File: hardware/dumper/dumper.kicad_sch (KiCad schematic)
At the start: 17 parts, among them J1 /Reset, J10 arduino 10, J11 ss, J2 Clock In, J3 data, J4 clock, J5 2816 /WR disconnect, J6 arduino 13, J7 arduino 11, J8 arduino 5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

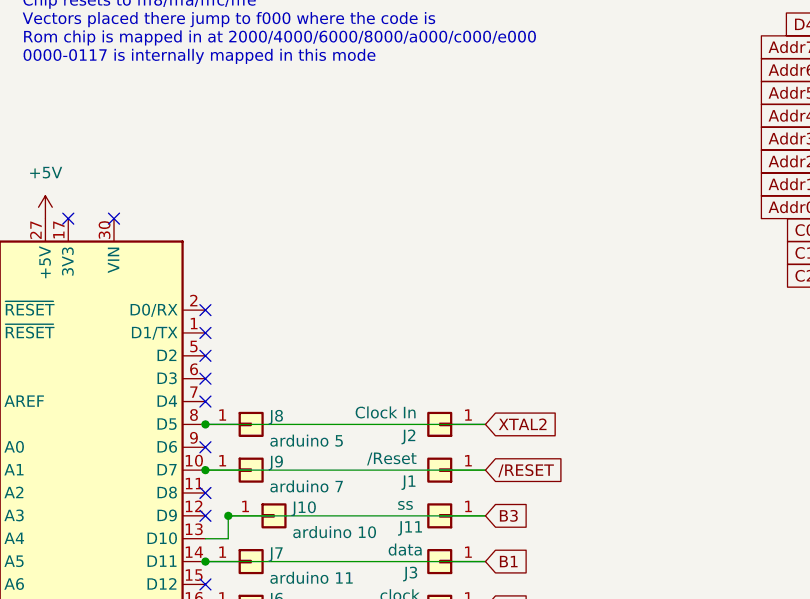
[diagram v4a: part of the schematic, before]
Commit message: added button and LED, still need software support though
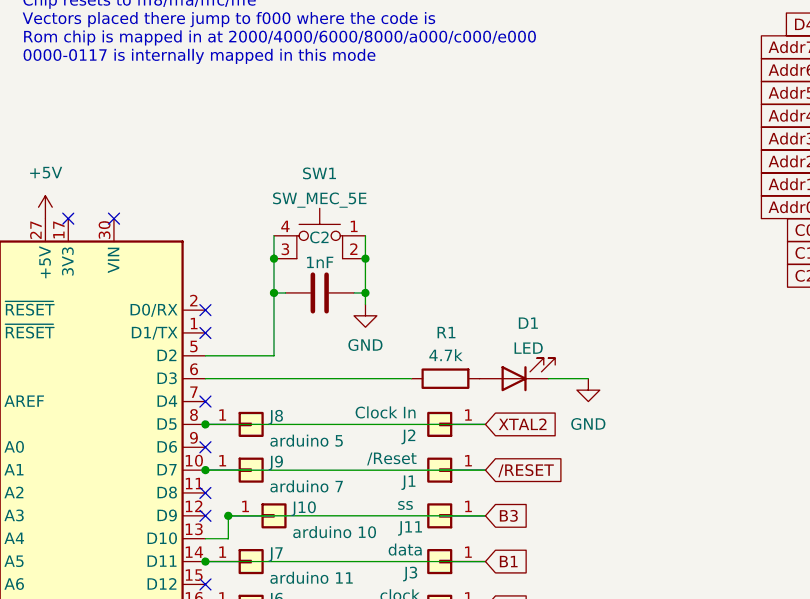
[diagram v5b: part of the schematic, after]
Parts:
- added C2: 1nF, Capacitor_THT:C_Axial_L3.8mm_D2.6mm_P7.50mm_Horizontal, symbol Device:C
- added D1: LED, LED_THT:LED_D5.0mm, symbol Device:LED
- added R1: 4.7k, Resistor_THT:R_Axial_DIN0207_L6.3mm_D2.5mm_P2.54mm_Vertical, symbol Device:R
- added SW1: SW_MEC_5E, Button_Switch_THT:SW_TH_Tactile_Omron_B3F-10xx, symbol Switch:SW_MEC_5E
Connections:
- net GND: now also C2.1, D1.1 (K), SW1.1, SW1.2
- net at A1.5 (D2): now also C2.2, SW1.3 (K), SW1.4 (A)
- net at A1.6 (D3): now also R1.1
- new net: D1.2 (A), R1.2
- no-connect marks 22 -> 20
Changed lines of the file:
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@@
   (junction (at 196.85 39.37) (diameter 0) (color 0 0 0 0)
   )
+  (junction (at 78.105 67.945) (diameter 0) (color 0 0 0 0)
+  )
   (junction (at 70.485 86.36) (diameter 0) (color 0 0 0 0)
   )
+  (junction (at 88.265 67.945) (diameter 0) (color 0 0 0 0)
+  )
   (junction (at 70.485 106.68) (diameter 0) (color 0 0 0 0)
   )
   (junction (at 70.485 91.44) (diameter 0) (color 0 0 0 0)
+  )
+  (junction (at 78.105 71.755) (diameter 0) (color 0 0 0 0)
+  )
+  (junction (at 88.265 71.755) (diameter 0) (color 0 0 0 0)
   )
   (junction (at 233.68 113.03) (diameter 0) (color 0 0 0 0)
@@
   (no_connect (at 70.485 93.98))
   (no_connect (at 70.485 96.52))
-  (no_connect (at 70.485 81.28))
-  (no_connect (at 70.485 78.74))
   (no_connect (at 70.485 83.82))
   (no_connect (at 60.325 63.5))
@@
     (stroke (width 0) (type default) (color 0 0 0 0))
   )
+  (wire (pts (xy 88.265 71.755) (xy 88.265 73.025))
+    (stroke (width 0) (type default) (color 0 0 0 0))
+  )
   (wire (pts (xy 70.485 106.68) (xy 101.6 106.68))
     (stroke (width 0) (type default) (color 0 0 0 0))
   )
+  (wire (pts (xy 88.265 65.405) (xy 88.265 67.945))
+    (stroke (width 0) (type default) (color 0 0 0 0))
+  )
+  (wire (pts (xy 78.105 71.755) (xy 78.105 67.945))
+    (stroke (width 0) (type default) (color 0 0 0 0))
+  )
   (wire (pts (xy 214.63 107.95) (xy 207.01 107.95))
     (stroke (width 0) (type default) (color 0 0 0 0))
@@
     (stroke (width 0) (type default) (color 0 0 0 0))
   )
+  (wire (pts (xy 78.105 78.74) (xy 70.485 78.74))
+    (stroke (width 0) (type default) (color 0 0 0 0))
+  )
   (wire (pts (xy 70.485 101.6) (xy 101.6 101.6))
     (stroke (width 0) (type default) (color 0 0 0 0))
@@
     (stroke (width 0) (type default) (color 0 0 0 0))
   )
+  (wire (pts (xy 78.105 65.405) (xy 78.105 67.945))
+    (stroke (width 0) (type default) (color 0 0 0 0))
+  )
   (wire (pts (xy 195.58 41.91) (xy 196.85 41.91))
     (stroke (width 0) (type default) (color 0 0 0 0))
   )
+  (wire (pts (xy 79.375 71.755) (xy 78.105 71.755))
+    (stroke (width 0) (type default) (color 0 0 0 0))
+  )
   (wire (pts (xy 139.7 36.195) (xy 139.7 39.37))
     (stroke (width 0) (type default) (color 0 0 0 0))
@@
   )
   (wire (pts (xy 55.245 121.285) (xy 55.245 114.3))
+    (stroke (width 0) (type default) (color 0 0 0 0))
+  )
+  (wire (pts (xy 88.265 71.755) (xy 86.995 71.755))
+    (stroke (width 0) (type default) (color 0 0 0 0))
+  )
+  (wire (pts (xy 93.345 81.28) (xy 70.485 81.28))
+    (stroke (width 0) (type default) (color 0 0 0 0))
+  )
+  (wire (pts (xy 113.03 81.28) (xy 108.585 81.28))
+    (stroke (width 0) (type default) (color 0 0 0 0))
+  )
+  (wire (pts (xy 88.265 67.945) (xy 88.265 71.755))
+    (stroke (width 0) (type default) (color 0 0 0 0))
+  )
+  (wire (pts (xy 78.105 71.755) (xy 78.105 78.74))
     (stroke (width 0) (type default) (color 0 0 0 0))
   )
@@
     (pin "2")
   )
+  (symbol (lib_id "Switch:SW_MEC_5E") (at 83.185 67.945 0) (mirror y) (unit 1)
+    (in_bom yes) (on_board yes) (fields_autoplaced)
+    (property "Reference" "SW1" (id 0) (at 83.185 58.5175 0))
+    (property "Value" "SW_MEC_5E" (id 1) (at 83.185 61.2926 0))
+    (property "Footprint" "Button_Switch_THT:SW_TH_Tactile_Omron_B3F-10xx" (id 2) (at 83.185 60.325 0)
+      (effects (font (size 1.27 1.27)) hide)
+    )
+    (property "Datasheet" "http://www.apem.com/int/index.php?controller=attachment&id_attachment=1371" (id 3) (at 83.185 60.325 0)
+      (effects (font (size 1.27 1.27)) hide)
+    )
+    (pin "1")
+    (pin "2")
+    (pin "3")
+    (pin "4")
+  )
   (symbol (lib_id "power:GND") (at 204.47 54.61 0) (unit 1)
     (in_bom yes) (on_board yes) (fields_autoplaced)
@@
     (pin "1")
   )
+  (symbol (lib_id "power:GND") (at 113.03 81.28 0) (unit 1)
+    (in_bom yes) (on_board yes) (fields_autoplaced)
+    (property "Reference" "#PWR0115" (id 0) (at 113.03 87.63 0)
+      (effects (font (size 1.27 1.27)) hide)
+    )
+    (property "Value" "GND" (id 1) (at 113.03 86.36 0))
+    (property "Footprint" "" (id 2) (at 113.03 81.28 0)
+      (effects (font (size 1.27 1.27)) hide)
+    )
+    (property "Datasheet" "" (id 3) (at 113.03 81.28 0)
+      (effects (font (size 1.27 1.27)) hide)
+    )
+    (pin "1")
+  )
   (symbol (lib_id "Connector_Generic:Conn_01x01") (at 75.565 106.68 0) (unit 1)
     (in_bom yes) (on_board yes) (fields_autoplaced)
@@
     )
     (pin "1")
+  )
+  (symbol (lib_id "Device:LED") (at 104.775 81.28 180) (unit 1)
+    (in_bom yes) (on_board yes) (fields_autoplaced)
+    (property "Reference" "D1" (id 0) (at 106.3625 75.1545 0))
+    (property "Value" "LED" (id 1) (at 106.3625 77.9296 0))
+    (property "Footprint" "LED_THT:LED_D5.0mm" (id 2) (at 104.775 81.28 0)
+      (effects (font (size 1.27 1.27)) hide)
+    )
+    (property "Datasheet" "~" (id 3) (at 104.775 81.28 0)
+      (effects (font (size 1.27 1.27)) hide)
+    )
+    (pin "1")
+    (pin "2")
   )
   (symbol (lib_id "power:+5V") (at 229.235 130.175 0) (unit 1)
@@
     )
     (pin "1")
+  )
+  (symbol (lib_id "Device:R") (at 97.155 81.28 90) (mirror x) (unit 1)
+    (in_bom yes) (on_board yes)
+    (property "Reference" "R1" (id 0) (at 98.425 76.2 90)
+      (effects (font (size 1.27 1.27)) (justify left))
+    )
+    (property "Value" "4.7k" (id 1) (at 99.06 78.74 90)
+      (effects (font (size 1.27 1.27)) (justify left))
+    )
+    (property "Footprint" "Resistor_THT:R_Axial_DIN0207_L6.3mm_D2.5mm_P2.54mm_Vertical" (id 2) (at 97.155 79.502 90)
+      (effects (font (size 1.27 1.27)) hide)
+    )
+    (property "Datasheet" "~" (id 3) (at 97.155 81.28 0)
+      (effects (font (size 1.27 1.27)) hide)
+    )
+    (pin "1")
+    (pin "2")
   )
   (symbol (lib_id "Connector_Generic:Conn_01x01") (at 96.52 101.6 180) (unit 1)
@@
     (pin "1")
   )
+  (symbol (lib_id "power:GND") (at 88.265 73.025 0) (mirror y) (unit 1)
+    (in_bom yes) (on_board yes) (fields_autoplaced)
+    (property "Reference" "#PWR0114" (id 0) (at 88.265 79.375 0)
+      (effects (font (size 1.27 1.27)) hide)
+    )
+    (property "Value" "GND" (id 1) (at 88.265 77.5875 0))
+    (property "Footprint" "" (id 2) (at 88.265 73.025 0)
+      (effects (font (size 1.27 1.27)) hide)
+    )
+    (property "Datasheet" "" (id 3) (at 88.265 73.025 0)
+      (effects (font (size 1.27 1.27)) hide)
+    )
+    (pin "1")
+  )
+  (symbol (lib_id "Device:C") (at 83.185 71.755 270) (mirror x) (unit 1)
+    (in_bom yes) (on_board yes) (fields_autoplaced)
+    (property "Reference" "C2" (id 0) (at 83.185 65.6295 90))
+    (property "Value" "1nF" (id 1) (at 83.185 68.4046 90))
+    (property "Footprint" "Capacitor_THT:C_Axial_L3.8mm_D2.6mm_P7.50mm_Horizontal" (id 2) (at 79.375 70.7898 0)
+      (effects (font (size 1.27 1.27)) hide)
+    )
+    (property "Datasheet" "~" (id 3) (at 83.185 71.755 0)
+      (effects (font (size 1.27 1.27)) hide)
+    )
+    (pin "1")
+    (pin "2")
+  )
   (symbol (lib_id "Connector_Generic:Conn_01x01") (at 96.52 106.68 180) (unit 1)
     (in_bom yes) (on_board yes)
@@
       (reference "#PWR0113") (unit 1) (value "+5V") (footprint "")
     )
+    (path "/caf3d6fa-4a2b-4403-b2a4-8ef75b254fa4"
+      (reference "#PWR0114") (unit 1) (value "GND") (footprint "")
+    )
+    (path "/1d761fca-95b7-43bf-972d-3e5ef51985f2"
+      (reference "#PWR0115") (unit 1) (value "GND") (footprint "")
+    )
     (path "/688ac639-00fc-4ac8-adf3-07f16d38668d"
       (reference "#PWR0116") (unit 1) (value "+5V") (footprint "")
@@
       (reference "C1") (unit 1) (value "0.1uF") (footprint "Capacitor_THT:C_Axial_L3.8mm_D2.6mm_P7.50mm_Horizontal")
     )
+    (path "/cbedcb1f-f6fd-4ef5-b1b7-a22936804498"
+      (reference "C2") (unit 1) (value "1nF") (footprint "Capacitor_THT:C_Axial_L3.8mm_D2.6mm_P7.50mm_Horizontal")
+    )
+    (path "/2fc6fbea-a5ac-44e1-ae14-5f7455ad4ad6"
+      (reference "D1") (unit 1) (value "LED") (footprint "LED_THT:LED_D5.0mm")
+    )
     (path "/8e871c2d-c01d-49fb-8a3b-6261894a19c0"
       (reference "J1") (unit 1) (value "/Reset") (footprint "Connector_PinHeader_2.54mm:PinHeader_1x01_P2.54mm_Vertical")
@@
       (reference "J11") (unit 1) (value "ss") (footprint "Connector_PinHeader_2.54mm:PinHeader_1x01_P2.54mm_Vertical")
     )
+    (path "/87fb4618-ffba-4098-894c-2a108e97e5a6"
+      (reference "R1") (unit 1) (value "4.7k") (footprint "Resistor_THT:R_Axial_DIN0207_L6.3mm_D2.5mm_P2.54mm_Vertical")
+    )
     (path "/010d4c25-3047-4e82-9722-4113a4b03be6"
       (reference "R2") (unit 1) (value "4.7k") (footprint "Resistor_THT:R_Axial_DIN0207_L6.3mm_D2.5mm_P2.54mm_Vertical")
     )
+    (path "/05b0e45b-bcdc-4c03-b4a1-c60becea55d5"
+      (reference "SW1") (unit 1) (value "SW_MEC_5E") (footprint "Button_Switch_THT:SW_TH_Tactile_Omron_B3F-10xx")
+    )
     (path "/5bab83de-2cb2-4fe3-8877-7d62e5b0d55c"

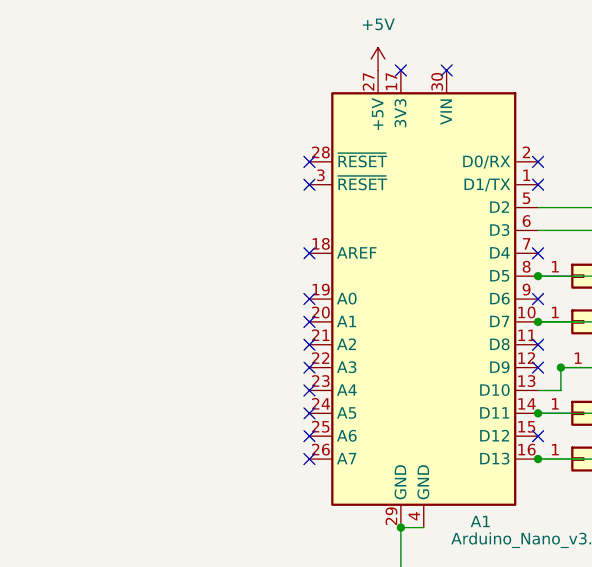
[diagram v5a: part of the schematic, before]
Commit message: added version B changes
silk update and analog sense wire
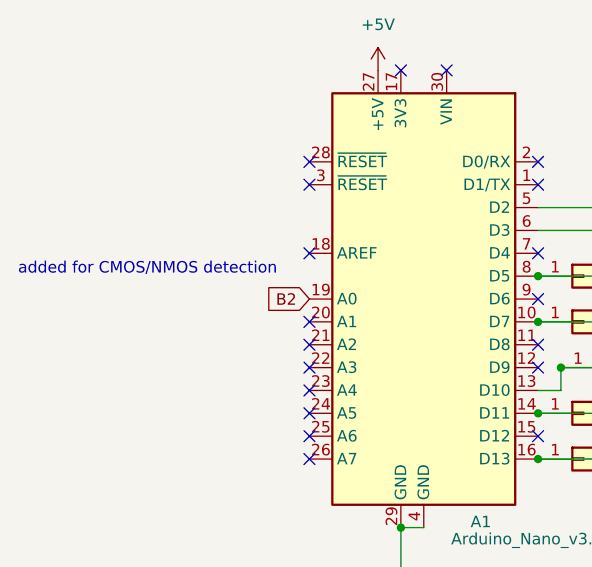
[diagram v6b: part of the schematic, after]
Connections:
- net B2: now also A1.19 (A0)
- no-connect marks 20 -> 19
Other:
- note added: "added for CMOS/NMOS detection"
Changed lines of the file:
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@@
   (no_connect (at 45.085 93.98))
   (no_connect (at 45.085 91.44))
-  (no_connect (at 45.085 88.9))
   (wire (pts (xy 55.245 114.3) (xy 57.785 114.3))
     (stroke (width 0) (type default) (color 0 0 0 0))
@@
     (effects (font (size 1.27 1.27)) (justify left bottom))
   )
+  (text "added for CMOS/NMOS detection" (at 12.7 86.36 0)
+    (effects (font (size 1.27 1.27)) (justify left bottom))
+  )
   (text "5v to pin 26 lets us use 2732/2716 roms" (at 198.12 44.45 0)
     (effects (font (size 1.27 1.27)) (justify left bottom))
@@
       (effects (font (size 1.27 1.27)) (justify right) hide)
     )
+  )
+  (global_label "B2" (shape input) (at 45.085 88.9 180) (fields_autoplaced)
+    (effects (font (size 1.27 1.27)) (justify right))
+    (property "Intersheet References" "${INTERSHEET_REFS}" (id 0) (at 40.1924 88.8206 0)
+      (effects (font (size 1.27 1.27)) (justify right) hide)
+    )

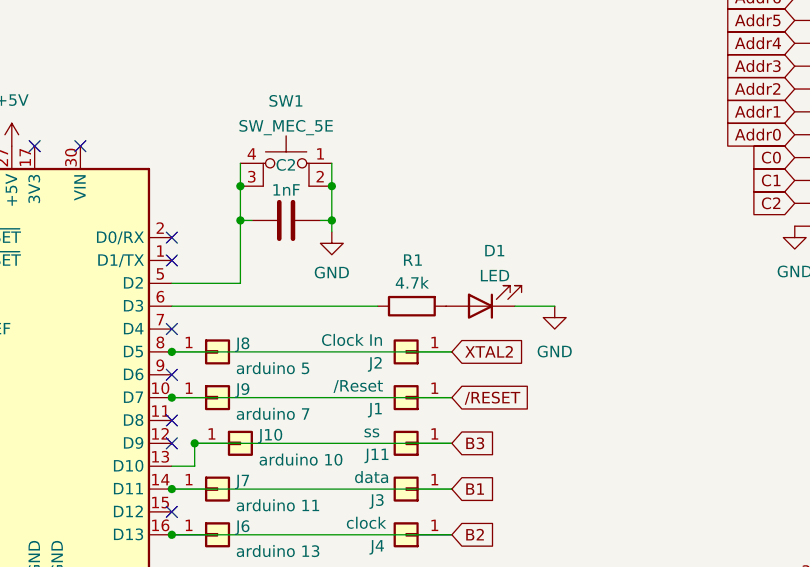
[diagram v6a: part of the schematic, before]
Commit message: fixed resistor value for LED
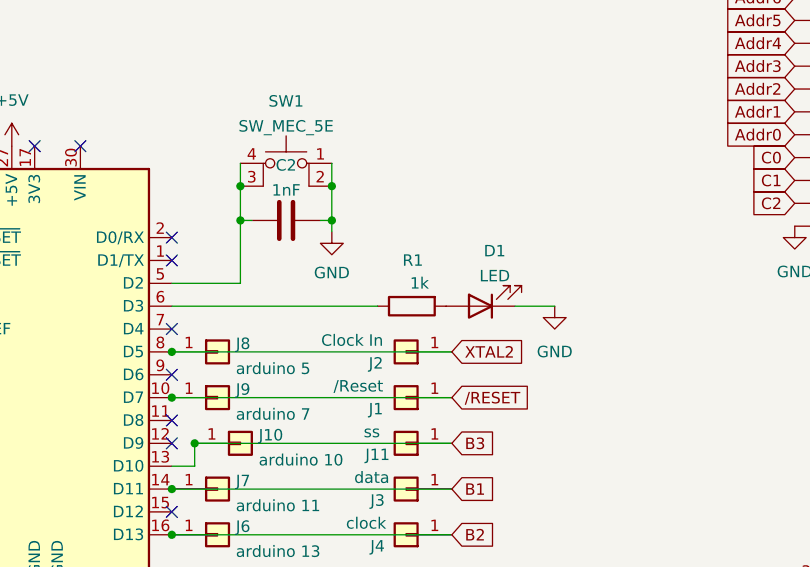
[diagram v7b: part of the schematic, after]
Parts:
- R1: value 4.7k -> 1k
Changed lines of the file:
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@@
       (effects (font (size 1.27 1.27)) (justify left))
     )
-    (property "Value" "4.7k" (id 1) (at 99.06 78.74 90)
+    (property "Value" "1k" (id 1) (at 99.06 78.74 90)
       (effects (font (size 1.27 1.27)) (justify left))
     )
@@
     )
     (path "/87fb4618-ffba-4098-894c-2a108e97e5a6"
-      (reference "R1") (unit 1) (value "4.7k") (footprint "Resistor_THT:R_Axial_DIN0207_L6.3mm_D2.5mm_P2.54mm_Vertical")
+      (reference "R1") (unit 1) (value "1k") (footprint "Resistor_THT:R_Axial_DIN0207_L6.3mm_D2.5mm_P2.54mm_Vertical")
     )
     (path "/010d4c25-3047-4e82-9722-4113a4b03be6"
